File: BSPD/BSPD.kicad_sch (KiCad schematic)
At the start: 65 parts, among them J2 282834-6, K2 G5Q-1A, Q1 BSS84, Q2 MMBT2222A, Q3 MMBT2222A, U1 LM339, U2 LM339, U3 74LVC2G00, U5 74LVC2G04, U6 LM311, U7 LM555xM, U8 74AHC1G32, U9 AMS1117-5.0

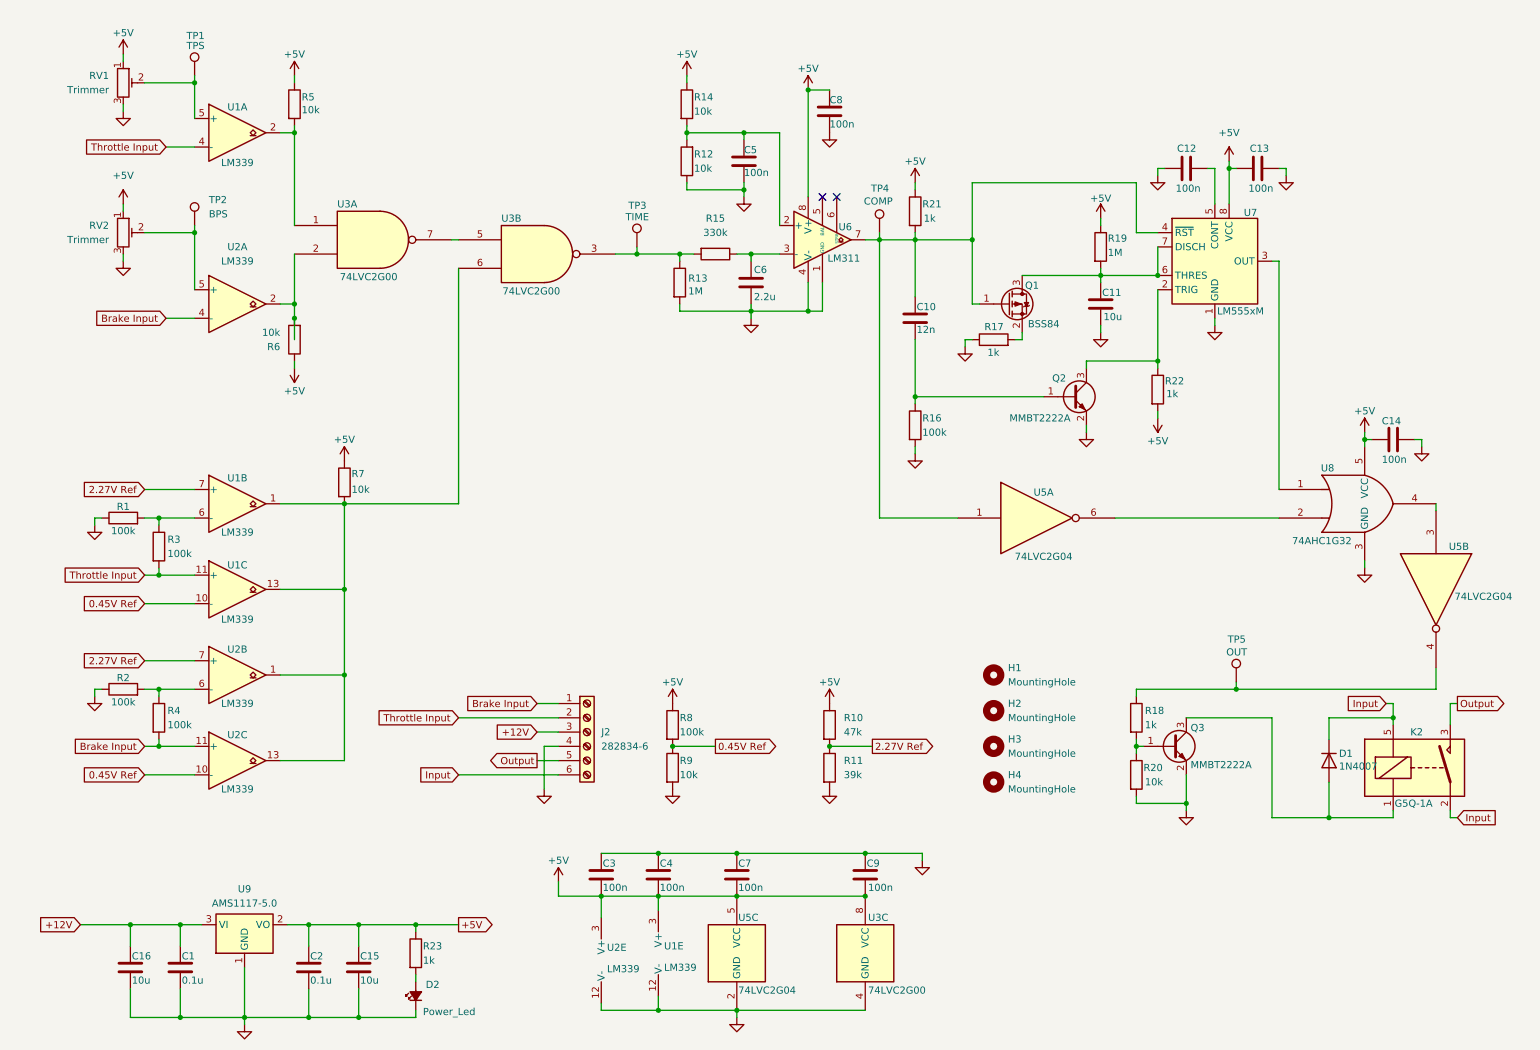
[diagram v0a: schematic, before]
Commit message: v0.2
updated design, fixed trimmers, added extra debug LEDs.
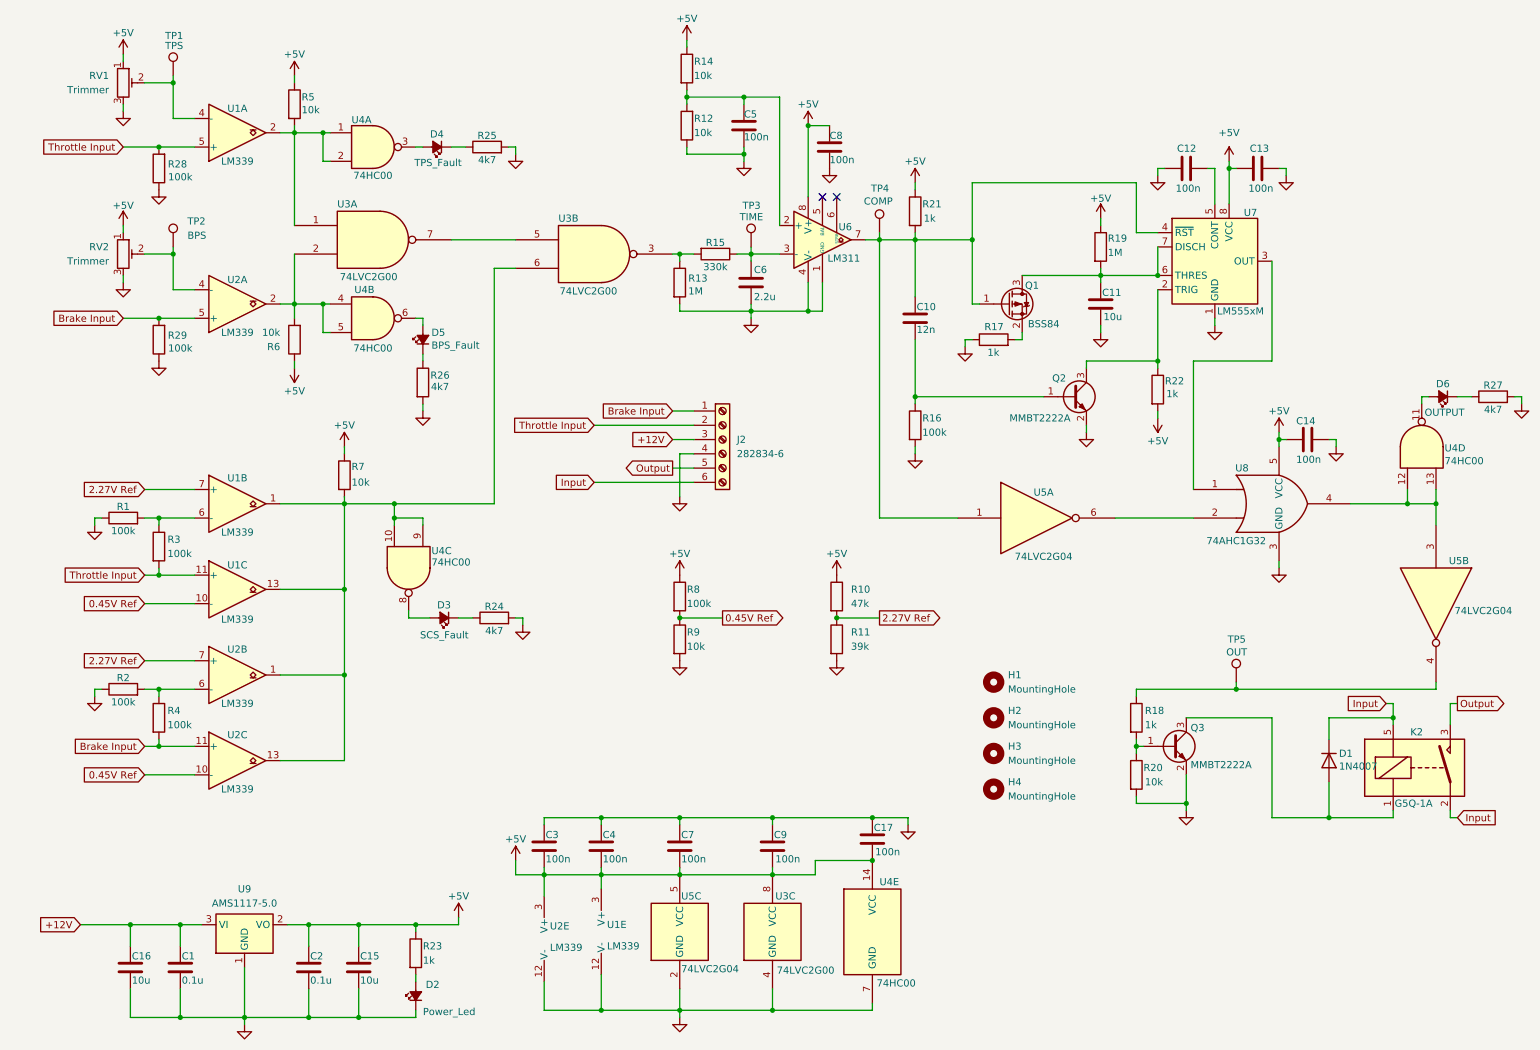
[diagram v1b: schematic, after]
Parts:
- added C17: 100n, Capacitor_SMD:C_0402_1005Metric, symbol Device:C
- added D3: SCS_Fault, LED_SMD:LED_0402_1005Metric, symbol Device:LED_Small_Filled
- added D4: TPS_Fault, LED_SMD:LED_0402_1005Metric, symbol Device:LED_Small_Filled
- added D5: BPS_Fault, LED_SMD:LED_0402_1005Metric, symbol Device:LED_Small_Filled
- added D6: OUTPUT, LED_SMD:LED_0402_1005Metric, symbol Device:LED_Small_Filled
- added R24, R25, R26, R27: 4k7, Resistor_SMD:R_0603_1608Metric, symbol Device:R
- added R28, R29: 100k, Resistor_SMD:R_0603_1608Metric, symbol Device:R
- added U4: 74HC00, 74HC00D_653:SOIC127P600X175-14N, symbol 74xx:74HC00
- D2: footprint LED_SMD:LED_0603_1608Metric -> LED_SMD:LED_0402_1005Metric
- H1, H2, H3, H4: footprint MountingHole:MountingHole_2.2mm_M2 -> MountingHole:MountingHole_2.2mm_M2_Pad
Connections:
- net +5V: now also C17.2, U4.14 (VCC)
- net Brake Input: now also U2.5 (+), R29.2; no longer U2.4 (-)
- net GND: now also C17.1, R24.2, R25.2, R26.2, R27.2, R28.1, R29.1, U4.7 (GND)
- net Throttle Input: now also U1.5 (+), R28.2; no longer U1.4 (-)
- net at R5.2, U1.2, U3.1: now also U4.1, U4.2
- net at R6.2, U2.2, U3.2: now also U4.4, U4.5
- net at R13.1, R15.2, U3.3: no longer TP3.1
- net at R7.2, U1.1, U1.13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: now also U4.10, U4.9
- net at C6.1, R15.1, U6.3 (-): now also TP3.1
- net at RV2.2, TP2.1: now also U2.4 (-); no longer U2.5 (+)
- net at U5.3, U8.4: now also U4.12, U4.13
- net at RV1.2, TP1.1: now also U1.4 (-); no longer U1.5 (+)
- new net: D3.1 (K), R24.1
- new net: D3.2 (A), U4.8
- new net: D4.1 (K), R25.1
- new net: D5.1 (K), R26.1
- new net: D5.2 (A), U4.6
- new net: D6.1 (K), R27.1
- new net: D4.2 (A), U4.3
- new net: D6.2 (A), U4.11
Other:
- moved on the sheet: C14, C3, C4, C5, C7, C8, C9, H1, H2, H3, H4, J2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

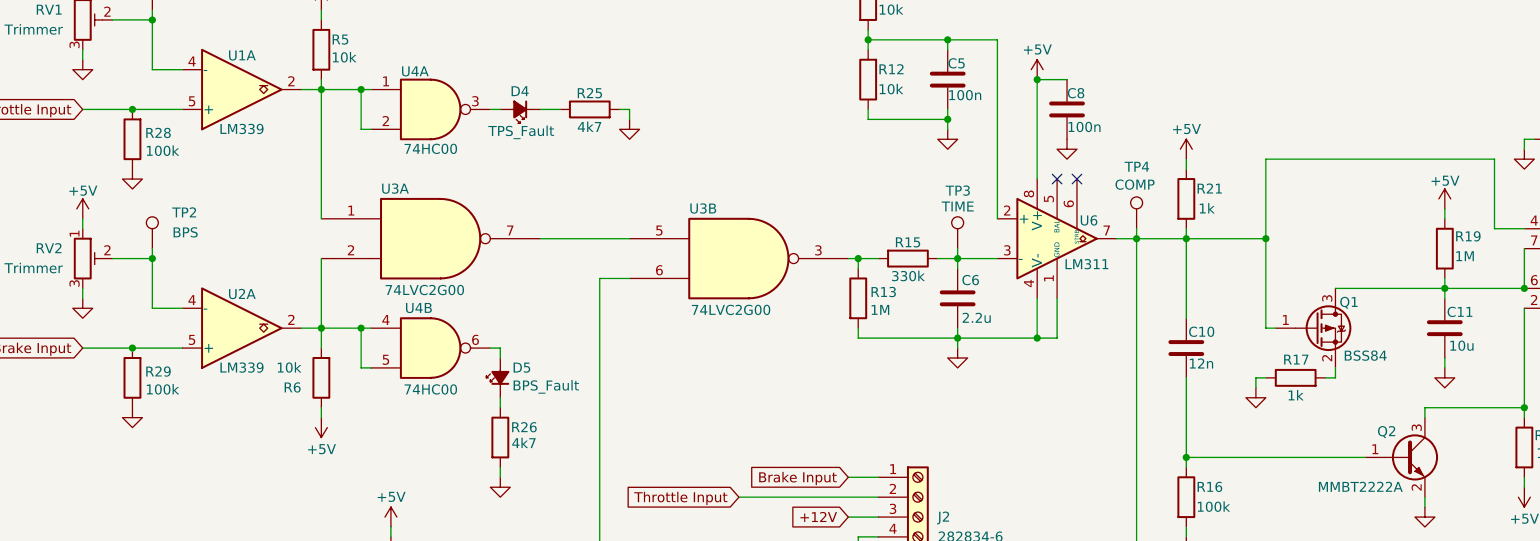
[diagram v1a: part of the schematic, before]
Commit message: minor resistor changes and symbol correction
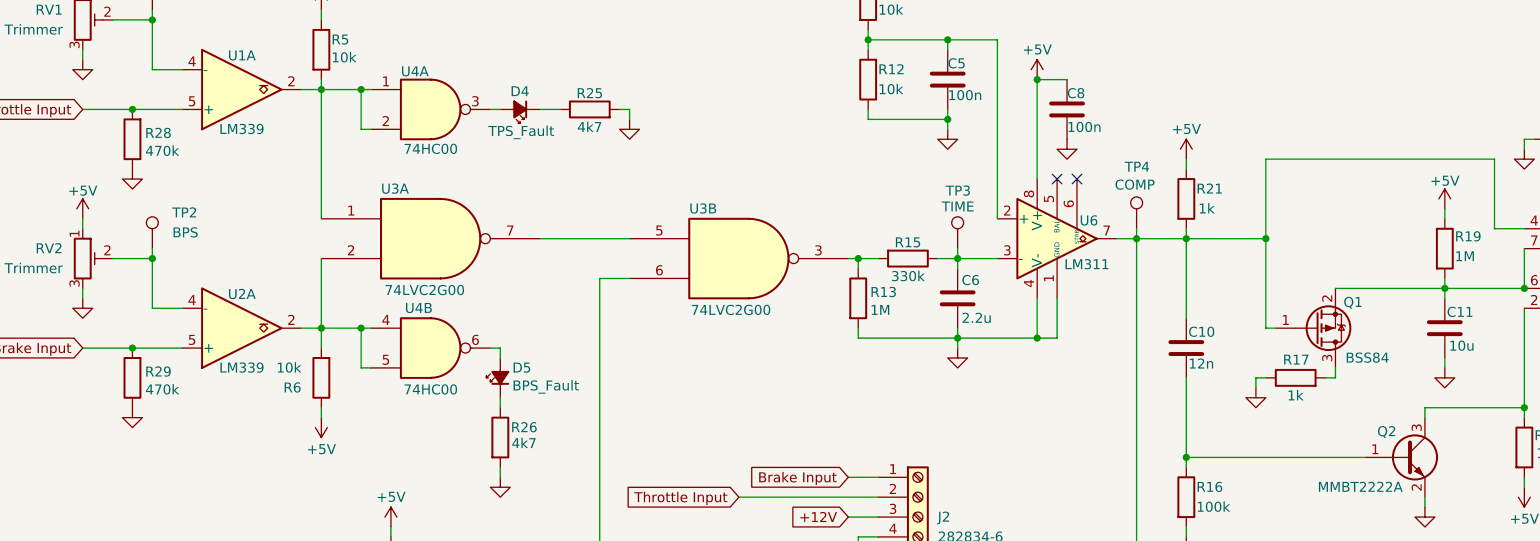
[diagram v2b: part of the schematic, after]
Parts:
- R28, R29: value 100k -> 470k
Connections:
- net at Q1.2 (S): now also C11.1, R19.2, U7.6 (THRES), U7.7 (DISCH); no longer R17.2
- new net: Q1.3 (D), R17.2
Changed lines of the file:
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@@
 		(lib_id "Transistor_FET:BSS84")
 		(at 189.23 64.77 0)
+		(mirror x)
 		(unit 1)
 		(exclude_from_sim no)
@@
 		(dnp no)
 		(property "Reference" "Q1"
-			(at 192.278 61.468 0)
+			(at 192.786 61.468 0)
 			(effects
 				(font
@@
 		)
 		(property "Value" "BSS84"
-			(at 192.786 68.326 0)
+			(at 193.04 68.58 0)
 			(effects
 				(font
@@
 		)
 		(property "Footprint" "Package_TO_SOT_SMD:SOT-23"
-			(at 194.31 66.675 0)
+			(at 194.31 62.865 0)
 			(effects
 				(font
@@
 		)
 		(property "Datasheet" "http://assets.nexperia.com/documents/data-sheet/BSS84.pdf"
-			(at 194.31 68.58 0)
+			(at 194.31 60.96 0)
 			(effects
 				(font
@@
 			)
 		)
-		(property "Value" "100k"
+		(property "Value" "470k"
 			(at 41.91 72.644 0)
 			(effects
@@
 			)
 		)
-		(property "Value" "100k"
+		(property "Value" "470k"
 			(at 41.91 42.164 0)
 			(effects

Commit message: minor changes
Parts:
- D2, D3, D4, D5, D6: footprint LED_SMD:LED_0402_1005Metric -> LED_SMD:LED_0603_1608Metric
- R23: value 1k -> 330
- R24, R25, R26, R27: value 4k7 -> 330
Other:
- moved on the sheet: C1, C15, C16, C2, D2, D6, H1, H2, H3, H4, J2, Q1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

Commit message: v0.4
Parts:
- added R30: 10k, Resistor_SMD:R_0603_1608Metric, symbol Device:R
- R18: value 1k -> 2.2k
- R23, R24, R25, R26, R27: value 330 -> 470
- R28, R29: value 470k -> 100k
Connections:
- net Brake Input: now also R30.2; no longer R4.2, U2.11 (+), U2.5 (+)
- net GND: no longer R20.2
- net Throttle Input: now also R20.2; no longer R3.2, U1.11 (+), U1.5 (+)
- net at Q3.1 (B), R18.2: no longer R20.1
- new net BPS: R30.1, R4.2, U2.11 (+), U2.5 (+)
- new net TPS: R20.1, R3.2, U1.11 (+), U1.5 (+)
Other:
- moved on the sheet: C17, C3, C4, C7, C9, Q3, R18, R28, R29, RV1, RV2
